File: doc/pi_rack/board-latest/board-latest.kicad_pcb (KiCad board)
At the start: 4 copper layers, 85 x 25 mm, 28 parts, among them J1 PI_POE, J2 PI_GPIO, J3 FAN, J4 AUX, Q1 2N7002, Q2 2N7002, Q3 DMG2305, U1 AG5300, U2 DS3231MZ, U3 SLS32AIA010MSUSON10XTMA2, U4 SK6812MINI-E, U5 SK6812MINI-E

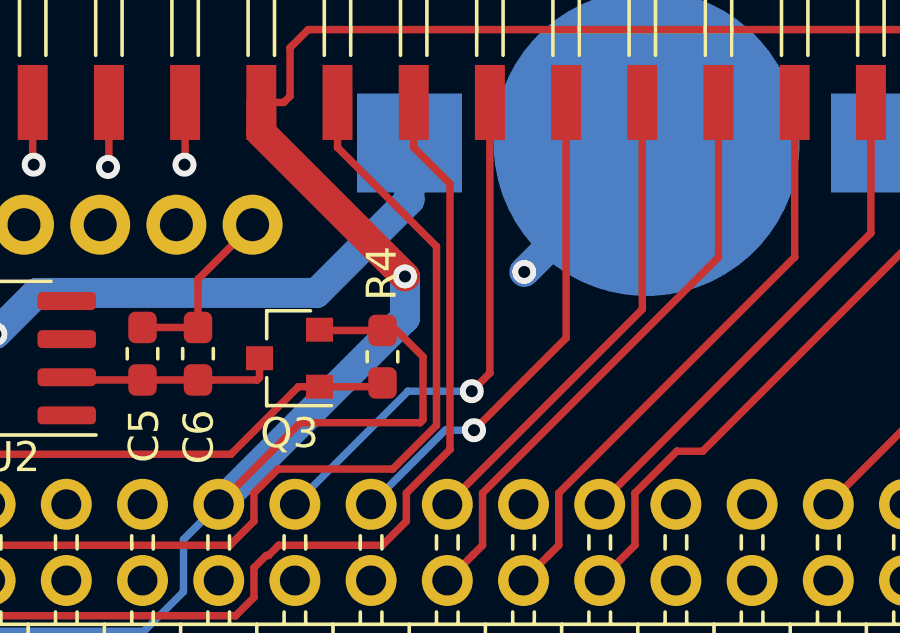
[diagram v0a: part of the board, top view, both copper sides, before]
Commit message: Migrate to Kicad 7 and add an image linter.
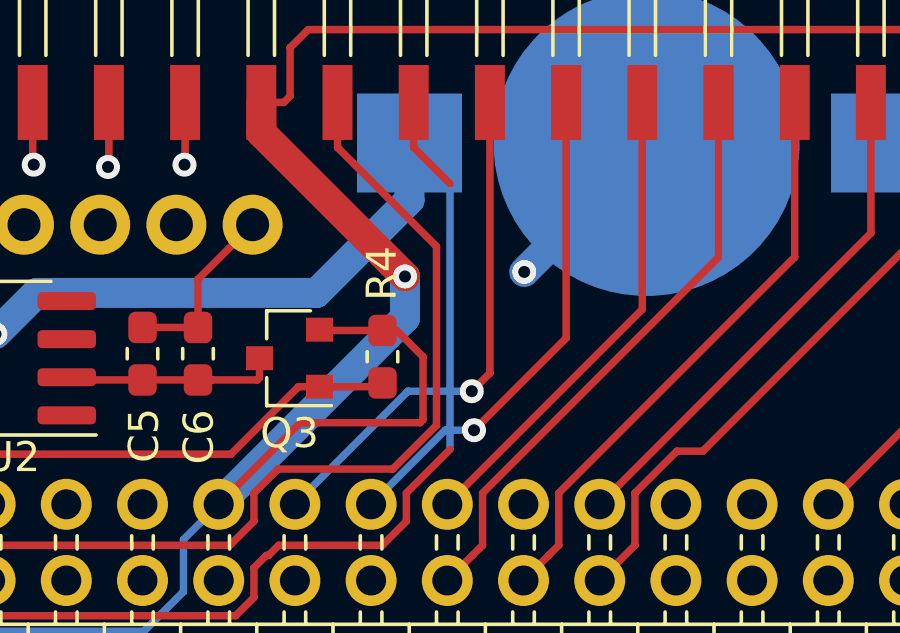
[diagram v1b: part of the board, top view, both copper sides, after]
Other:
- net class Default removed
